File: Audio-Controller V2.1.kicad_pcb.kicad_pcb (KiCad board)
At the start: 2 copper layers, 73 x 100 mm, 16 parts

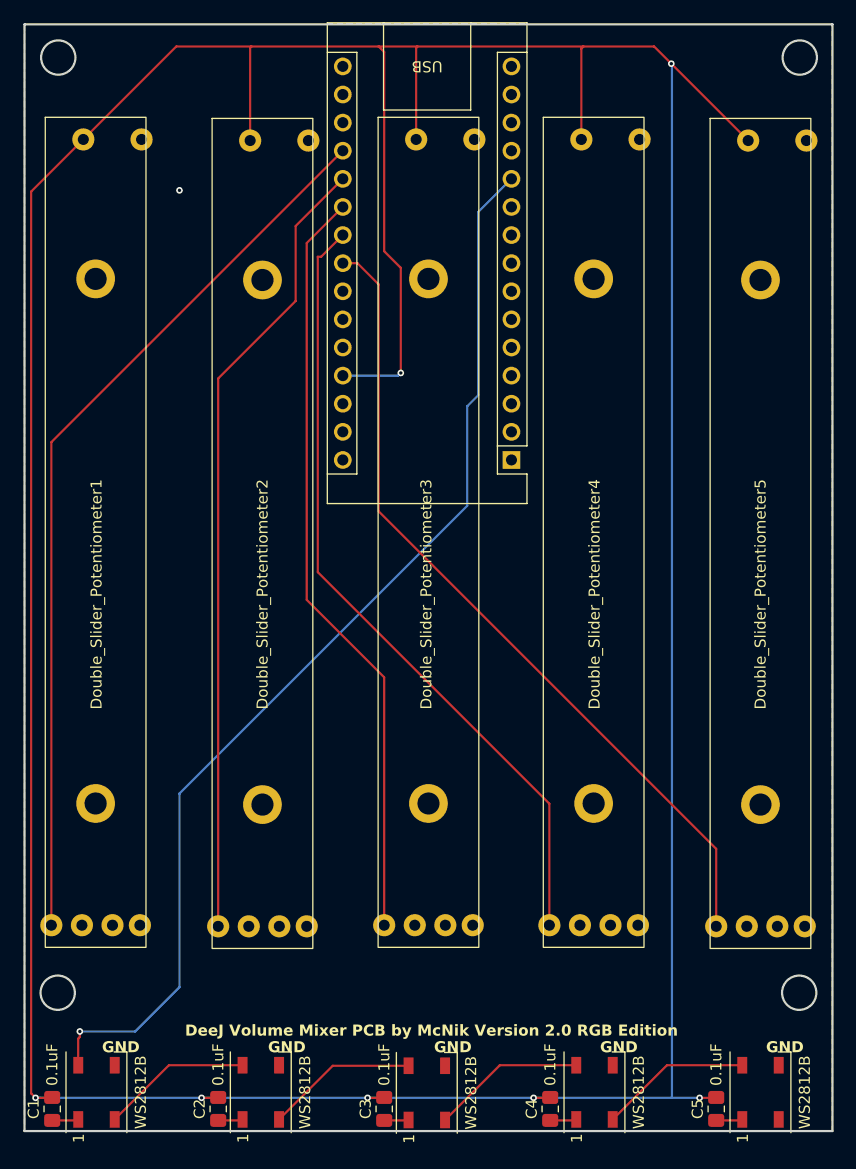
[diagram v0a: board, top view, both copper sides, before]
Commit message: Version 2.1
Fixed errors and tested design.
Working code included.
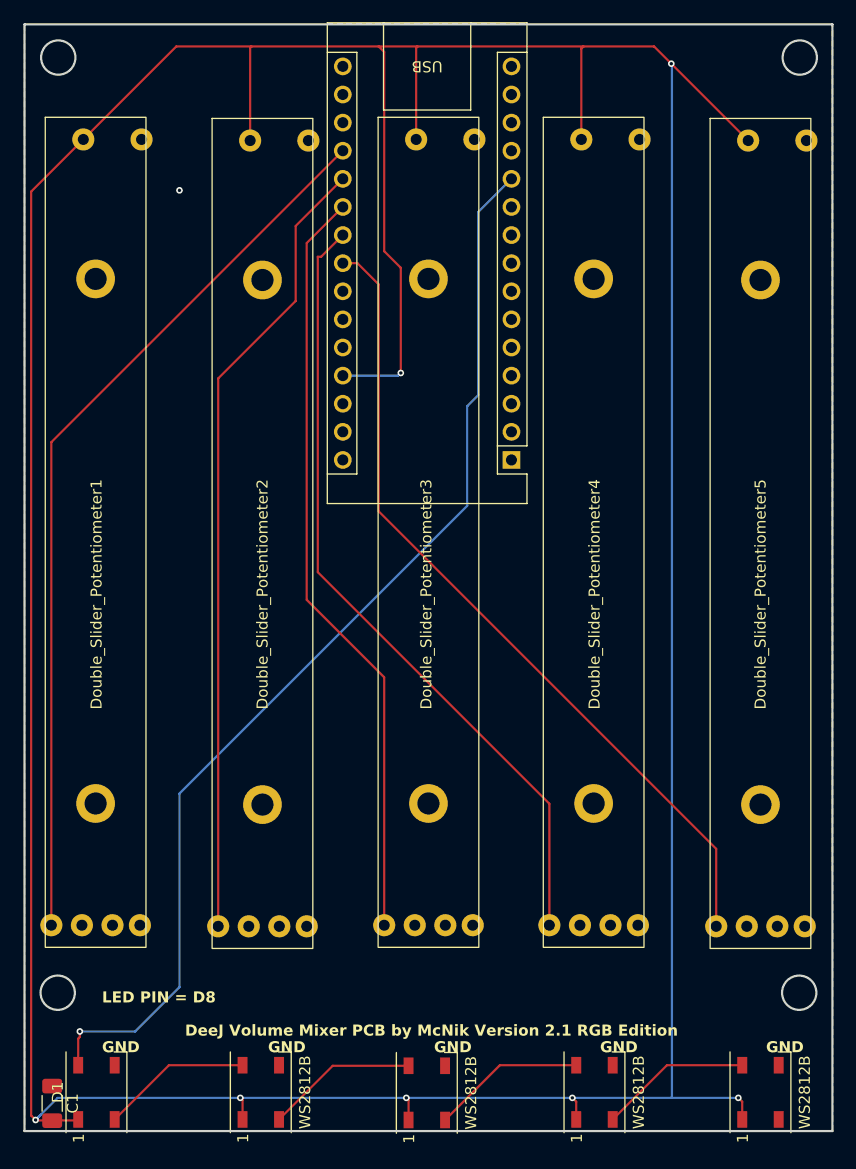
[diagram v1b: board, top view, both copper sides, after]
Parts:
- removed C2, C3, C4, C5: 0.1uF, Capacitor_SMD:C_0805_2012Metric_Pad1.18x1.45mm_HandSolder
- C1: footprint Capacitor_SMD:C_0805_2012Metric_Pad1.18x1.45mm_HandSolder -> Capacitor_SMD:C_1206_3216Metric_Pad1.33x1.80mm_HandSolder
- moved C1 0.50 mm to (50.5, 114.0), turned to -90 degrees
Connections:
- C1 pad 1: Net-(D1-VDD) -> GND
- D1 pad 1: Net-(D1-VDD) -> +5V
- D2 pad 1: Net-(D2-VDD) -> +5V
- D3 pad 1: Net-(D3-VDD) -> +5V
- D4 pad 1: Net-(D4-VDD) -> +5V
- D5 pad 1: Net-(D5-VDD) -> +5V
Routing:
- net +5V: track 378.5 -> 390.2 mm
- net Net-(D1-VDD): track 2.39 -> 0.00 mm
- net Net-(D5-VDD): track 2.39 -> 0.00 mm
- net Net-(D4-VDD): track 2.39 -> 0.00 mm
- net Net-(D2-VDD): track 2.24 -> 0.00 mm
- net Net-(D3-VDD): track 2.22 -> 0.00 mm
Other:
- board text added: "DeeJ Volume Mixer PCB by McNik Version 2.1 RGB Edition"
- board text added: "LED PIN = D8"
- board text removed: "DeeJ Volume Mixer PCB by McNik Version 2.0 RGB Edition"

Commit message: small corrections
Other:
- board text added: "0.1uF"
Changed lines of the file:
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@@
 		)
 		(property "Value" "0.1uF"
-			(at 0 1.85 90)
-			(layer "F.Fab")
-			(effects
-				(font
-					(size 1 1)
-					(thickness 0.15)
+			(at -4.5 0 90)
+			(layer "F.SilkS")
+			(effects
+				(font
+					(size 1 1)
+					(thickness 0.2)
+					(bold yes)
 				)
 			)
@@
 		(layer "F.SilkS")
 		(effects
+			(font
+				(size 1 1)
+				(thickness 0.2)
+				(bold yes)
+			)
+			(justify left bottom)
+		)
+	)
+	(gr_text "0.1uF"
+		(at 51 111.5 90)
+		(layer "F.SilkS")
+		(effects
